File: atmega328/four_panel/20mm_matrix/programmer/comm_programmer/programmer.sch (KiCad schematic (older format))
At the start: 3 parts, among them P1 CONN_2, P2 CONN_3X2, P3 CONN15

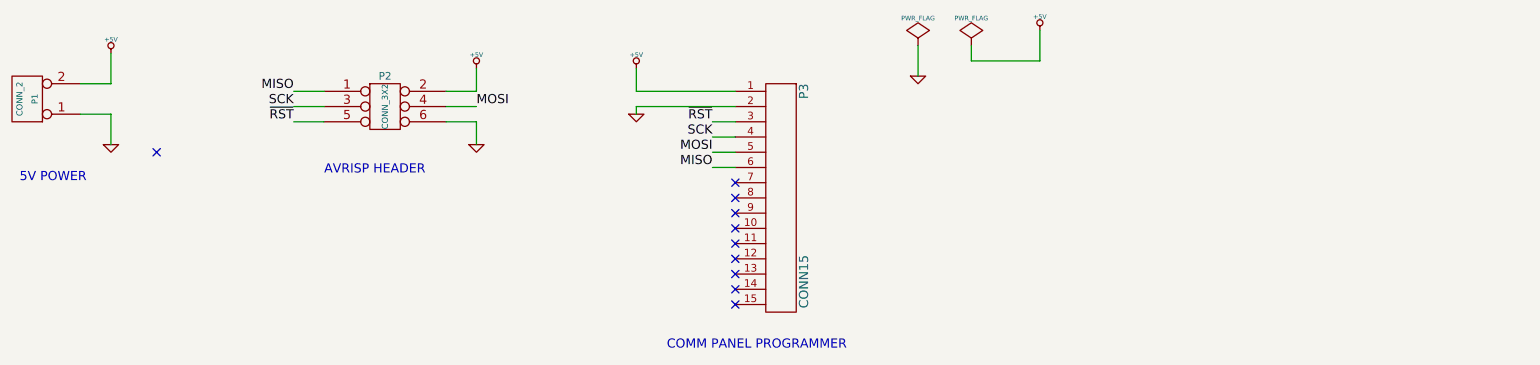
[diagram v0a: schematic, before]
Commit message: Added bottom pcb for 4x20mm atmega328 panel driver.
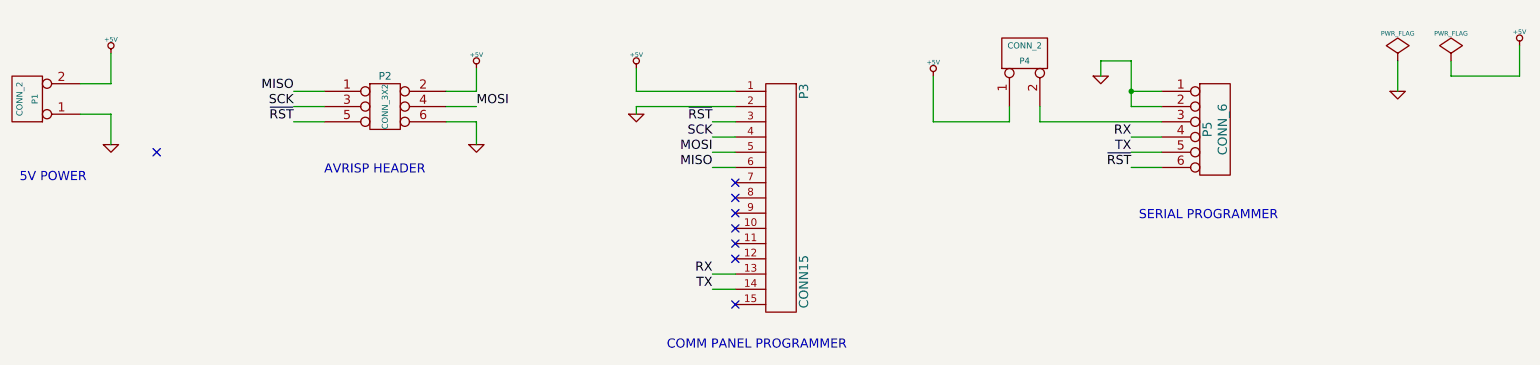
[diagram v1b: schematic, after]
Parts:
- added P4: CONN_2, symbol CONN_2
- added P5: CONN_6, symbol CONN_6
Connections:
- net +5V: now also P4.1 (P1)
- net GND: now also P5.1, P5.2
- net ~RST: now also P5.6
- net RX: now reaches P3.13
- net RX: now also P5.4
- net TX: now reaches P3.14
- net TX: now also P5.5
- new net: P4.2 (PM), P5.3
- no-connect marks 10 -> 8
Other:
- note added: "SERIAL PROGRAMMER"
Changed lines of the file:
@@
 NoConn ~ 5800 2250
 NoConn ~ 5800 2350
-NoConn ~ 5800 2450
-NoConn ~ 5800 2550
 NoConn ~ 5800 2650
 NoConn ~ 2000 1650
@@
 L PWR_FLAG #FLG07
 U 1 1 5240BBF0
-P 7350 950
-F 0 "#FLG07" H 7350 1045 30  0001 C CNN
-F 1 "PWR_FLAG" H 7350 1130 30  0000 C CNN
-F 2 "" H 7350 950 60  0000 C CNN
-F 3 "" H 7350 950 60  0000 C CNN
-	1    7350 950
+P 10500 1050
+F 0 "#FLG07" H 10500 1145 30  0001 C CNN
+F 1 "PWR_FLAG" H 10500 1230 30  0000 C CNN
+F 2 "" H 10500 1050 60  0000 C CNN
+F 3 "" H 10500 1050 60  0000 C CNN
+	1    10500 1050
 	1    0    0    -1
 $EndComp
@@
 L +5V #PWR08
 U 1 1 5240BBFF
-P 7800 850
-F 0 "#PWR08" H 7800 940 20  0001 C CNN
-F 1 "+5V" H 7800 940 30  0000 C CNN
-F 2 "" H 7800 850 60  0000 C CNN
-F 3 "" H 7800 850 60  0000 C CNN
-	1    7800 850
+P 10950 950
+F 0 "#PWR08" H 10950 1040 20  0001 C CNN
+F 1 "+5V" H 10950 1040 30  0000 C CNN
+F 2 "" H 10950 950 60  0000 C CNN
+F 3 "" H 10950 950 60  0000 C CNN
+	1    10950 950
 	1    0    0    -1
 $EndComp
 Wire Wire Line
-	7350 950  7350 1050
+	10500 1050 10500 1150
 Wire Wire Line
-	7350 1050 7800 1050
+	10500 1150 10950 1150
 Wire Wire Line
-	7800 1050 7800 850
+	10950 1150 10950 950
 $Comp
 L GND #PWR09
 U 1 1 5240BC2F
-P 7000 1150
-F 0 "#PWR09" H 7000 1150 30  0001 C CNN
-F 1 "GND" H 7000 1080 30  0001 C CNN
-F 2 "" H 7000 1150 60  0000 C CNN
-F 3 "" H 7000 1150 60  0000 C CNN
-	1    7000 1150
+P 10150 1250
+F 0 "#PWR09" H 10150 1250 30  0001 C CNN
+F 1 "GND" H 10150 1180 30  0001 C CNN
+F 2 "" H 10150 1250 60  0000 C CNN
+F 3 "" H 10150 1250 60  0000 C CNN
+	1    10150 1250
 	1    0    0    -1
 $EndComp
@@
 L PWR_FLAG #FLG010
 U 1 1 5240BC44
-P 7000 950
-F 0 "#FLG010" H 7000 1045 30  0001 C CNN
-F 1 "PWR_FLAG" H 7000 1130 30  0000 C CNN
-F 2 "" H 7000 950 60  0000 C CNN
-F 3 "" H 7000 950 60  0000 C CNN
-	1    7000 950
+P 10150 1050
+F 0 "#FLG010" H 10150 1145 30  0001 C CNN
+F 1 "PWR_FLAG" H 10150 1230 30  0000 C CNN
+F 2 "" H 10150 1050 60  0000 C CNN
+F 3 "" H 10150 1050 60  0000 C CNN
+	1    10150 1050
 	1    0    0    -1
 $EndComp
 Wire Wire Line
-	7000 950  7000 1150
+	10150 1050 10150 1250
+$Comp
+L CONN_6 P5
+U 1 1 524129A8
+P 8950 1500
+F 0 "P5" V 8900 1500 60  0000 C CNN
+F 1 "CONN_6" V 9000 1500 60  0000 C CNN
+F 2 "" H 8950 1500 60  0000 C CNN
+F 3 "" H 8950 1500 60  0000 C CNN
+	1    8950 1500
+	1    0    0    -1
+$EndComp
+Text Notes 8450 2100 0    60   ~ 0
+SERIAL PROGRAMMER
+Wire Wire Line
+	8400 1350 8600 1350
+Wire Wire Line
+	8400 1250 8600 1250
+Connection ~ 8400 1250
+Wire Wire Line
+	8400 1050 8400 1350
+Wire Wire Line
+	8400 1050 8200 1050
+Wire Wire Line
+	8200 1050 8200 1150
+$Comp
+L GND #PWR?
+U 1 1 52412B0B
+P 8200 1150
+F 0 "#PWR?" H 8200 1150 30  0001 C CNN
+F 1 "GND" H 8200 1080 30  0001 C CNN
+F 2 "" H 8200 1150 60  0000 C CNN
+F 3 "" H 8200 1150 60  0000 C CNN
+	1    8200 1150
+	1    0    0    -1
+$EndComp
+$Comp
+L CONN_2 P4
+U 1 1 52412B1A
+P 7700 1000
+F 0 "P4" V 7650 1000 40  0000 C CNN
+F 1 "CONN_2" V 7750 1000 40  0000 C CNN
+F 2 "" H 7700 1000 60  0000 C CNN
+F 3 "" H 7700 1000 60  0000 C CNN
+	1    7700 1000
+	0    -1   -1   0
+$EndComp
+Wire Wire Line
+	8600 1450 7800 1450
+Wire Wire Line
+	7800 1450 7800 1350
+Wire Wire Line
+	7600 1350 7600 1450
+Wire Wire Line
+	7600 1450 7100 1450
+Wire Wire Line
+	7100 1450 7100 1150
+$Comp
+L +5V #PWR?
+U 1 1 52412B6A
+P 7100 1150
+F 0 "#PWR?" H 7100 1240 20  0001 C CNN
+F 1 "+5V" H 7100 1240 30  0000 C CNN
+F 2 "" H 7100 1150 60  0000 C CNN
+F 3 "" H 7100 1150 60  0000 C CNN
+	1    7100 1150
+	1    0    0    -1
+$EndComp
+Wire Wire Line
+	5800 2450 5650 2450
+Wire Wire Line
+	5800 2550 5650 2550
+Text Label 5650 2450 2    60   ~ 0
+RX
+Text Label 5650 2550 2    60   ~ 0
+TX
+Wire Wire Line
+	8600 1550 8400 1550
+Wire Wire Line
+	8600 1650 8400 1650
+Text Label 8400 1550 2    60   ~ 0
+RX
+Text Label 8400 1650 2    60   ~ 0
+TX
+Wire Wire Line
+	8600 1750 8400 1750
+Text Label 8400 1750 2    60   ~ 0
+~RST
 $EndSCHEMATC
